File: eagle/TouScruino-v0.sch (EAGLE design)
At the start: 42 parts, among them J1 AVR_ISP, Q1 8MHz, Q2 MMBT2222A, Q3 8MHz, U1 ATMEGA1284P, U2 PJ28004C, U3 ARDUINO_SHIELD, U4 MCP73831, U5 MIC5209-3.3YS, X1 USBSMD

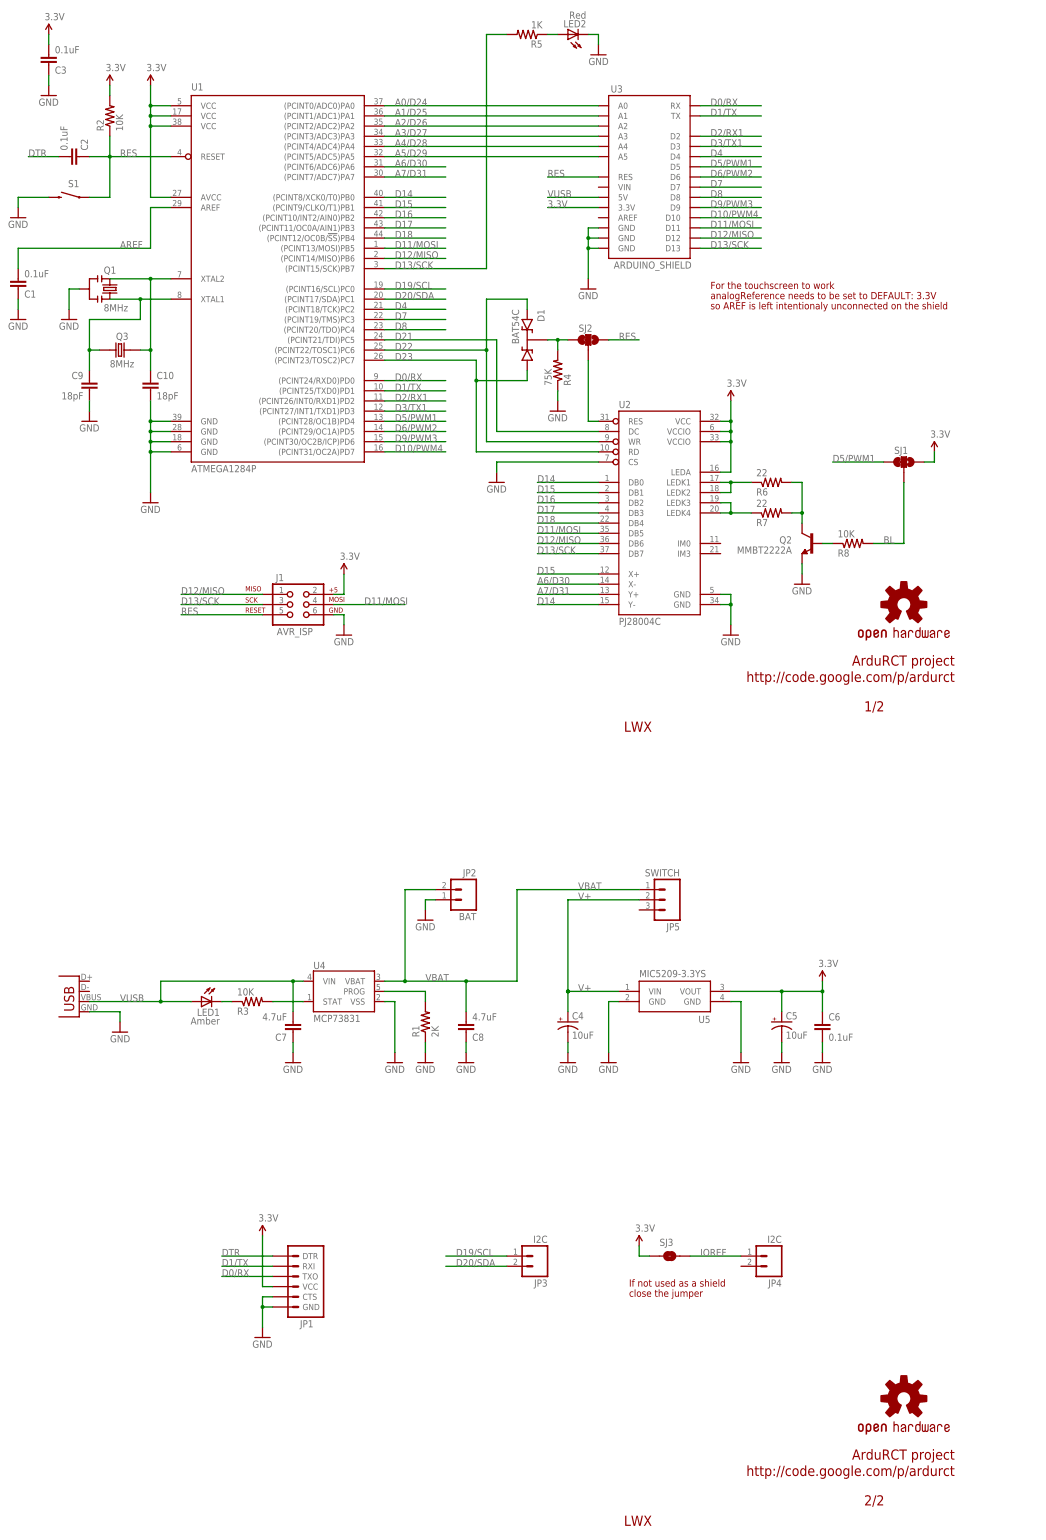
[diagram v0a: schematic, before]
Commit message: 
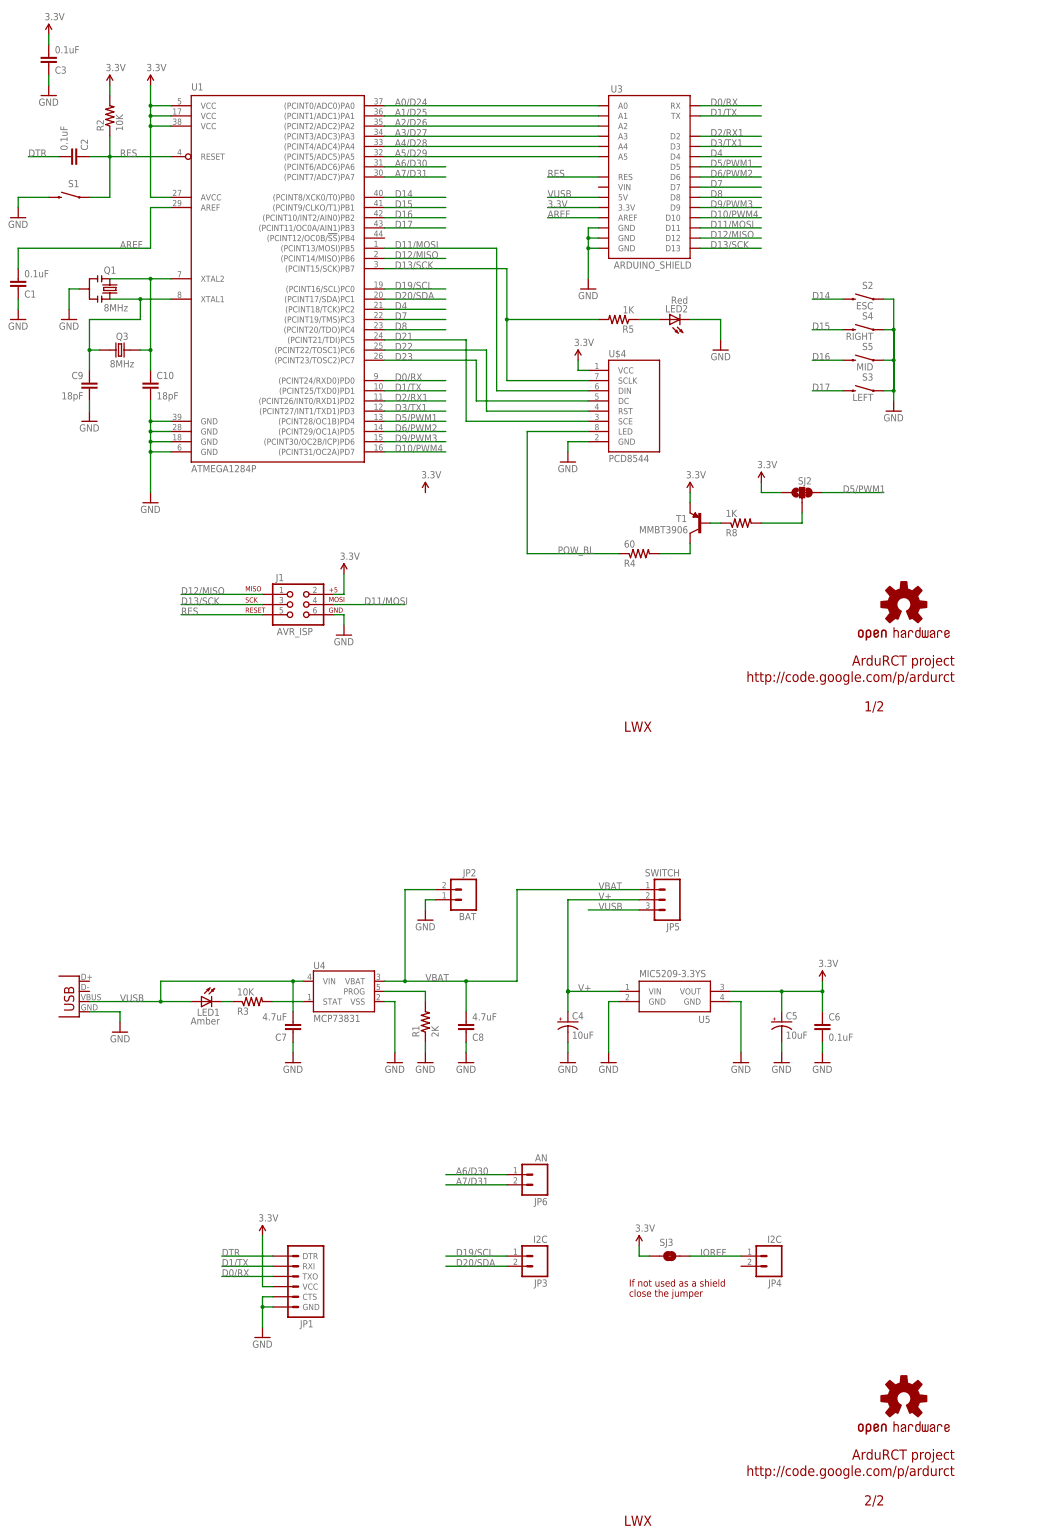
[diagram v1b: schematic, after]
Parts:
- removed D1: BAT54C, wibauxl:BAT54C
- removed Q2: MMBT2222A, SparkFun:TRANSISTOR_NPNSOT23-3
- removed R6, R7: 22, SparkFun:RESISTOR0805-RES
- removed SJ1: SJ_2WAYS_1-2, wibauxl:SJ_2WAYS_1-2
- removed U2: PJ28004C, wibauxl:PJ28004C
- added JP6: AN, wibauxl:M02
- added S2: ESC, wibauxl:SWITCH_SMD
- added S3: LEFT, wibauxl:SWITCH_SMD
- added S4: RIGHT, wibauxl:SWITCH_SMD
- added S5: MID, wibauxl:SWITCH_SMD
- added T1: MMBT3906, wibauxl:TRANSISTOR_PNPSMD
- added U$4: PCD8544, wibauxl:PCD8544
- R4: value 75K -> 60
- R8: value 10K -> 1K
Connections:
- removed net BL: R8.2, SJ1.2
- removed net D18: U1.(PCINT12/OC0B/!SS!)PB4, U2.DB4
- removed net LCD_RES: SJ2.2, U2.RES
- removed net N$25: R7.1, U2.LEDK3, U2.LEDK4
- removed net N$32: R6.1, U2.LEDK1, U2.LEDK2
- removed net N$4: Q2.B, R8.1
- removed net N$7: Q2.C, R6.2, R7.2
- removed net N$9: D1.K, R4.2, SJ2.1
- new net BL_CMD: R8.2, SJ2.2
- new net N$17: R4.2, T1.C
- new net N$27: R8.1, T1.B
- new net POW_BL: R4.1, U$4.LED
- net 3.3V: now also SJ2.3, T1.E, U$4.VCC; no longer SJ1.3, U2.LEDA, U2.VCC, U2.VCCIO@1, U2.VCCIO@2
- net A6/D30: now also JP6.1; no longer U2.X-
- net A7/D31: now also JP6.2; no longer U2.Y+
- net AREF: now also U3.AREF
- net D11/MOSI: now also U$4.DIN; no longer U2.DB5
- net D12/MISO: no longer U2.DB6
- net D13/SCK: now also U$4.SCLK; no longer U2.DB7
- net D14: now also S2.2; no longer U2.DB0, U2.Y-
- net D15: now also S4.2; no longer U2.DB1, U2.X+
- net D16: now also S5.2; no longer U2.DB2
- net D17: now also S3.2; no longer U2.DB3
- net D21: now also U$4.SCE; no longer U2.DC
- net D22: now also U$4.RST; no longer D1.A2, U2.WR
- net D23: now also U$4.DC; no longer D1.A1, U2.RD
- net D5/PWM1: now also SJ2.1; no longer SJ1.1
- net GND: now also S2.1, S3.1, S4.1, S5.1, U$4.GND; no longer Q2.E, R4.1, U2.CS, U2.GND@1, U2.GND@2
- net RES: no longer SJ2.3
- net VUSB: now also JP5.3
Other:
- note removed: "For the touchscreen to work"
- note removed: "analogReference needs to be set to DEFAULT: 3.3V"
- note removed: "so AREF is left intentionaly unconnected on the shield"
- moved on the sheet: LED2, R4, R5, R8, SJ2
